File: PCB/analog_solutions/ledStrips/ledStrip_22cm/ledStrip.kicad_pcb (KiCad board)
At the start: 2 copper layers, 220 x 10 mm, 45 parts, among them J1 Conn_01x01_Pin, J2 Conn_01x01_Pin, J3 Conn_01x01_Pin, J4 Conn_01x01_Pin, J5 Conn_01x01_Pin, J6 Conn_01x01_Pin, U1 LM317_TO-252

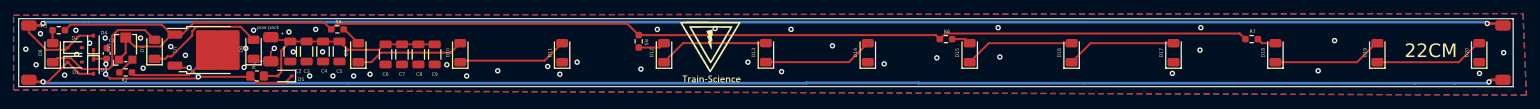
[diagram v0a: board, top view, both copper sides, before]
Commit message: Changed all 4 LED strips with 500R potentiometer and warm white 0805 LEDS Also put production files in RELEASE folder
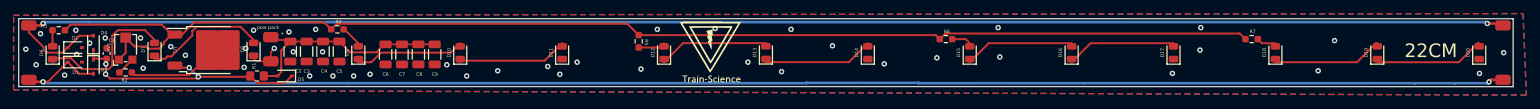
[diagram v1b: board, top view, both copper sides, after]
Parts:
- D10, D11, D12, D13, D14, D15, D16, D17, D18, D19, D20, D6, D7, D8, D9: footprint LED_SMD:LED_1206_3216Metric -> LED_SMD:LED_0805_2012Metric
- RV1: value 200R -> 500R
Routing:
- net AC1: track 229.9 -> 230.4 mm
